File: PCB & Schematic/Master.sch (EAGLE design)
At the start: 25 parts, among them M1 ARDUINO_R3_ICSP_NODIM, X1 MAB5SH, X2 MAB5SH

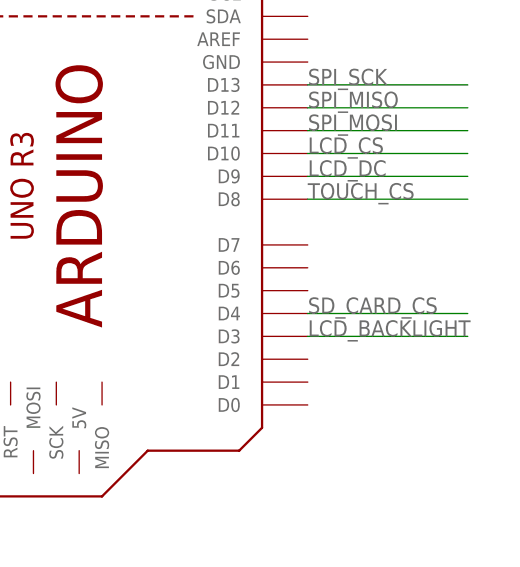
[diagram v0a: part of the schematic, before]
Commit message: Fix backlight dimming on capacitive TS.
Adafruit's schematic (or my understanding of it?) was wrong, and the
capacitive touchscreen uses digital pin 5 for backlight dimming, not
digital pin 3.

Since most pins are unused, just hooking pins 3 and 5 together works
fine, and requires no other changes. Now the PCB supports either TS.
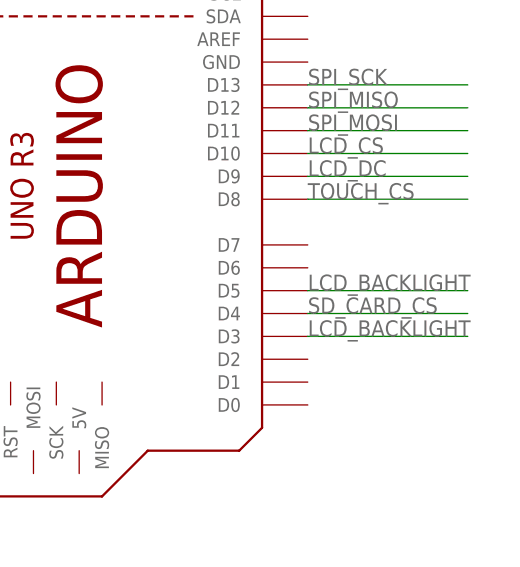
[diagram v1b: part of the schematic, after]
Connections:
- net LCD_BACKLIGHT: now also M1.D5
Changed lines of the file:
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@@
 <label x="2.54" y="7.62" size="1.778" layer="95"/>
+</segment>
+<segment>
+<pinref part="M1" gate="G$1" pin="D5"/>
+<wire x1="259.08" y1="38.1" x2="276.86" y2="38.1" width="0.1524" layer="91"/>
+<label x="259.08" y="38.1" size="1.778" layer="95"/>
 </segment>
 </net>
